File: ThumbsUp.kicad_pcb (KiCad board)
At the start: 2 copper layers, 211.3 x 232.1 mm, 56 parts, among them J1 52559-1233, J1L1 PJ-3200B, J1R1 PJ-3200B, J2 52559-1233, U1 ProMicro

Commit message: v12: Branch: Made the thumb keys reversible - split their hinges, so they could be flipped over.
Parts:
- added H26: MountingHole_Pad, MountingHole:MountingHole_3.5mm_Pad, F.Cu at (55.8, 123.8)
- added H28: MountingHole_Pad, MountingHole:MountingHole_3.5mm_Pad, F.Cu at (71.2, 123.8)
- added H29: MountingHole_Pad, MountingHole:MountingHole_3.5mm_Pad, F.Cu at (55.7, 253.8)
- added H30: MountingHole_Pad, MountingHole:MountingHole_3.5mm_Pad, F.Cu at (71.2, 253.8)
- added MX1: SwE, footprints:SW_D2FC_OMR, F.Cu at (55.8, 114.6)
- added MX2: SwU, footprints:SW_D2FC_OMR, F.Cu at (71.3, 114.6)
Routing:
- net GND-P: track 44.5 -> 0.00 mm, vias 2 -> 0
- net (no net): track 0.00 -> 44.5 mm, vias 0 -> 2
- net GND: track 602.3 -> 633.8 mm
- net SwU: track 64.1 -> 86.9 mm
- net SwE: track 61.1 -> 80.2 mm
- net GNDA: track 222.5 -> 217.5 mm
- removed copper zone on B.Cu, net GND-P
- removed copper zone on F.Cu, net GND-P
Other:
- board size 211.3 x 232.1 mm -> 211.3 x 242.6 mm
- board text added: "u/ak66666 ThumbsUp! v.12 rev.6 July 2026"
- board text removed: "u/ak66666 ThumbsUp! v.12 rev.5 June 2026"

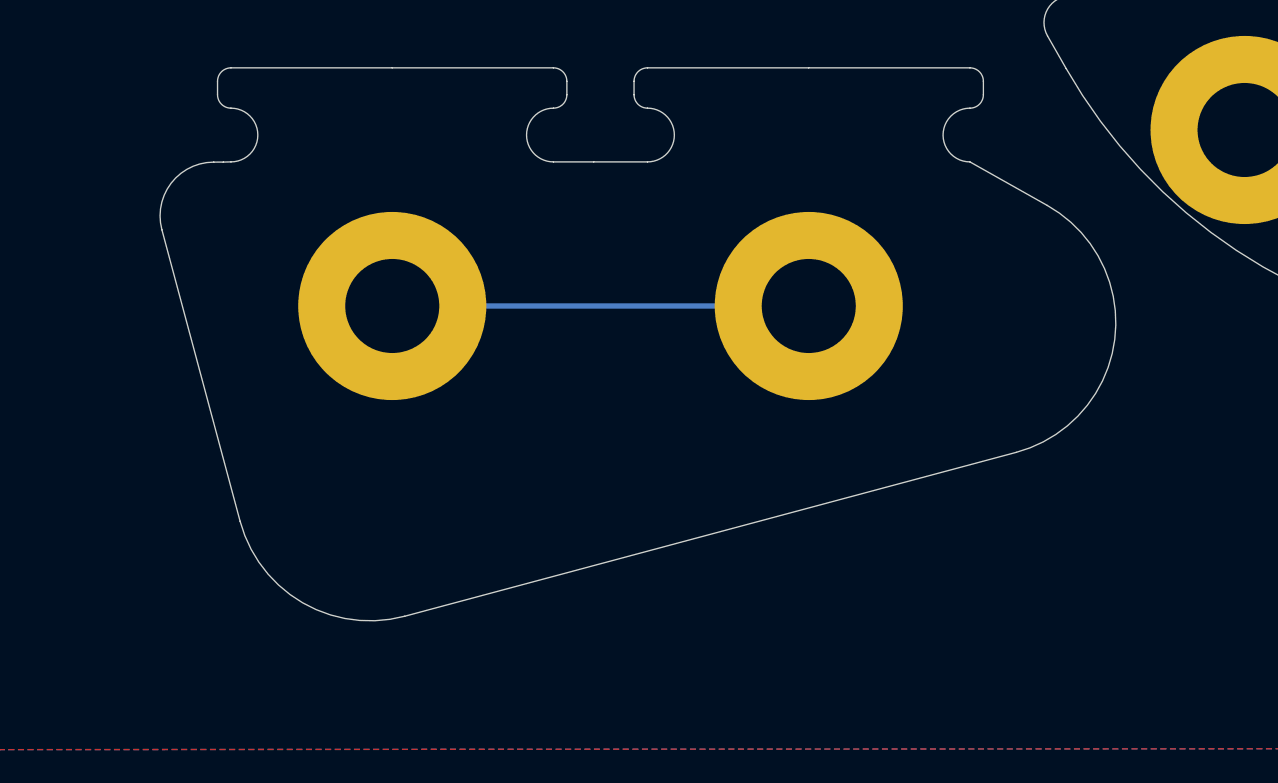
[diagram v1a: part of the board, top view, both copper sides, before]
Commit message: v12: Branch: Made the thumb key hinges replaceable - one board instead of two.
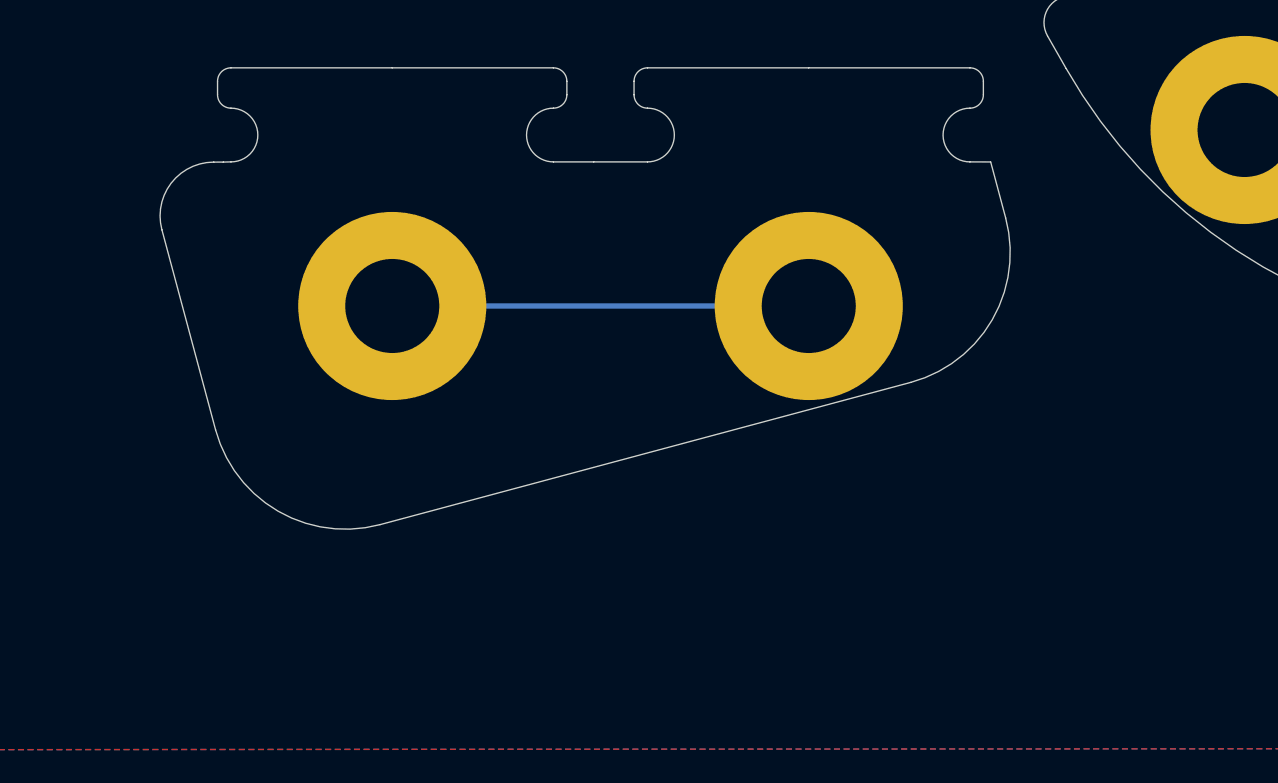
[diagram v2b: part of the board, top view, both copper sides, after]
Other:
- board size 211.3 x 242.6 mm -> 211.3 x 239.2 mm
- board text added: "THIS PCB IS NOT NEEDED, USE THE ONE BELOW FOR THE REVERSED THUMB KEYS"
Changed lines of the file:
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@@
 			)
 			(layer "F.CrtYd")
-			(net 118891357)
 		)
 		(fp_line
@@
 			)
 			(layer "F.CrtYd")
-			(net 118891357)
 		)
 		(fp_line
@@
 			)
 			(layer "F.CrtYd")
-			(net 118891357)
 		)
 		(fp_line
@@
 			)
 			(layer "F.CrtYd")
-			(net 118891357)
 		)
 		(fp_line
@@
 			)
 			(layer "F.Fab")
-			(net 118891357)
 		)
 		(fp_line
@@
 			)
 			(layer "F.Fab")
-			(net 118891357)
 		)
 		(fp_line
@@
 			)
 			(layer "F.Fab")
-			(net 118891357)
 		)
 		(fp_line
@@
 			)
 			(layer "F.Fab")
-			(net 118891357)
 		)
 		(fp_line
@@
 			)
 			(layer "F.Fab")
-			(net 118891357)
 		)
 		(fp_line
@@
 			)
 			(layer "F.Fab")
-			(net 118891357)
 		)
 		(fp_line
@@
 			)
 			(layer "F.Fab")
-			(net 118891357)
 		)
 		(fp_line
@@
 			)
 			(layer "F.Fab")
-			(net 118891357)
 		)
 		(fp_poly
@@
 			(fill yes)
 			(layer "F.Fab")
-			(net 118891357)
 		)
 		(fp_text user "*"
@@
 			)
 			(layer "F.CrtYd")
-			(net 118891357)
 		)
 		(fp_line
@@
 			)
 			(layer "F.CrtYd")
-			(net 118891357)
 		)
 		(fp_line
@@
 			)
 			(layer "F.CrtYd")
-			(net 118891357)
 		)
 		(fp_line
@@
 			)
 			(layer "F.CrtYd")
-			(net 118891357)
 		)
 		(fp_line
@@
 			)
 			(layer "F.Fab")
-			(net 118891357)
 		)
 		(fp_line
@@
 			)
 			(layer "F.Fab")
-			(net 118891357)
 		)
 		(fp_line
@@
 			)
 			(layer "F.Fab")
-			(net 118891357)
 		)
 		(fp_line
@@
 			)
 			(layer "F.Fab")
-			(net 118891357)
 		)
 		(fp_line
@@
 			)
 			(layer "F.Fab")
-			(net 118891357)
 		)
 		(fp_line
@@
 			)
 			(layer "F.Fab")
-			(net 118891357)
 		)
 		(fp_line
@@
 			)
 			(layer "F.Fab")
-			(net 118891357)
 		)
 		(fp_line
@@
 			)
 			(layer "F.Fab")
-			(net 118891357)
 		)
 		(fp_poly
@@
 			(fill yes)
 			(layer "F.Fab")
-			(net 118891357)
 		)
 		(fp_text user "*"
@@
 			(fill no)
 			(layer "Cmts.User")
-			(net 118891357)
 		)
 		(fp_circle
@@
 			(fill no)
 			(layer "F.CrtYd")
-			(net 118891357)
 		)
 		(fp_text user "${REFERENCE}"
@@
 			(fill no)
 			(layer "Cmts.User")
-			(net 118891357)
 		)
 		(fp_circle
@@
 			(fill no)
 			(layer "F.CrtYd")
-			(net 118891357)
 		)
 		(fp_text user "${REFERENCE}"
@@
 	)
 	(gr_arc
-		(start 80.129555 250.009425)
-		(mid 82.638051 254.992037)
-		(end 78.971608 259.196337)
-		(stroke
-			(width 0.05)
-			(type default)
-		)
-		(layer "Edge.Cuts")
-	)
-	(gr_arc
 		(start 114.968747 236.203553)
 		(mid 114.61518 236.05712)
@@
 	)
 	(gr_line
+		(start 78.02 248.39)
+		(end 78.577267 250.471467)
+		(stroke
+			(width 0.05)
+			(type default)
+		)
+		(layer "Edge.Cuts")
+	)
+	(gr_line
 		(start 120.968747 234.703553)
 		(end 114.968747 234.703553)
@@
 		(layer "Edge.Cuts")
 	)
-	(gr_line
-		(start 77.248 248.38772)
-		(end 80.129555 250.009425)
-		(stroke
-			(width 0.05)
-			(type default)
-		)
-		(layer "Edge.Cuts")
-	)
 	(gr_arc
 		(start 231.3 133.9)
@@
 	)
 	(gr_line
-		(start 50.08804 261.761925)
+		(start 49.173356 258.352387)
 		(end 47.177628 250.913603)
 		(stroke
@@
 	)
 	(gr_line
+		(start 77.248 248.38772)
+		(end 78.02 248.39)
+		(stroke
+			(width 0.05)
+			(type default)
+		)
+		(layer "Edge.Cuts")
+	)
+	(gr_line
 		(start 87.468747 238.703553)
 		(end 81.468747 238.703553)
@@
 		(layer "Edge.Cuts")
 	)
-	(gr_arc
-		(start 56.211595 265.295958)
-		(mid 52.418028 264.796943)
-		(end 50.088041 261.761925)
-		(stroke
-			(width 0.05)
-			(type default)
-		)
-		(layer "Edge.Cuts")
-	)
 	(gr_line
 		(start 218.8 91.4)
@@
 	)
 	(gr_arc
+		(start 55.296949 261.886326)
+		(mid 51.503383 261.387363)
+		(end 49.173356 258.352387)
+		(stroke
+			(width 0.05)
+			(type default)
+		)
+		(layer "Edge.Cuts")
+	)
+	(gr_arc
 		(start 160.468747 242.703553)
 		(mid 160.822287 242.850013)
@@
 	)
 	(gr_arc
+		(start 78.577267 250.471467)
+		(mid 78.077353 254.264864)
+		(end 75.041832 256.594096)
+		(stroke
+			(width 0.05)
+			(type default)
+		)
+		(layer "Edge.Cuts")
+	)
+	(gr_arc
 		(start 148.4683 174.5)
 		(mid 149.4683 175.5)
@@
 	)
 	(gr_line
-		(start 78.971608 259.196337)
-		(end 56.211595 265.295957)
+		(start 75.041832 256.594096)
+		(end 55.296949 261.886326)
 		(stroke
 			(width 0.05)
@@
 		)
 	)
+	(gr_text "THIS PCB IS NOT NEEDED,\nUSE THE ONE BELOW \nFOR THE REVERSED THUMB KEYS"
+		(at 19.54 222.66 0)
+		(layer "Edge.Cuts")
+		(effects
+			(font
+				(size 1 1)
+				(thickness 0.15)
+			)
+			(justify left bottom)
+		)
+	)

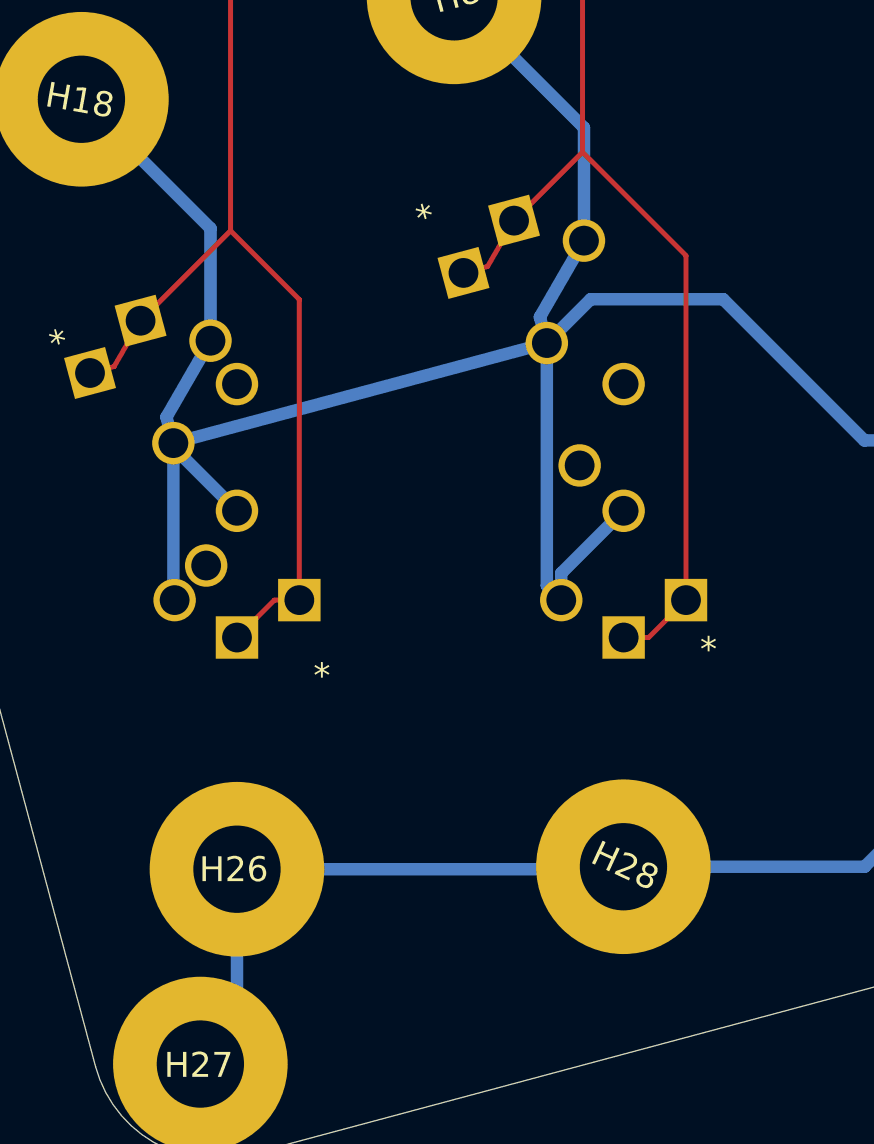
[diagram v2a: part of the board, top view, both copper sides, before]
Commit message: v12: Branch: Shifted the reversed thumb keys 1.5 down to fit the key paddles, there was not enough space.
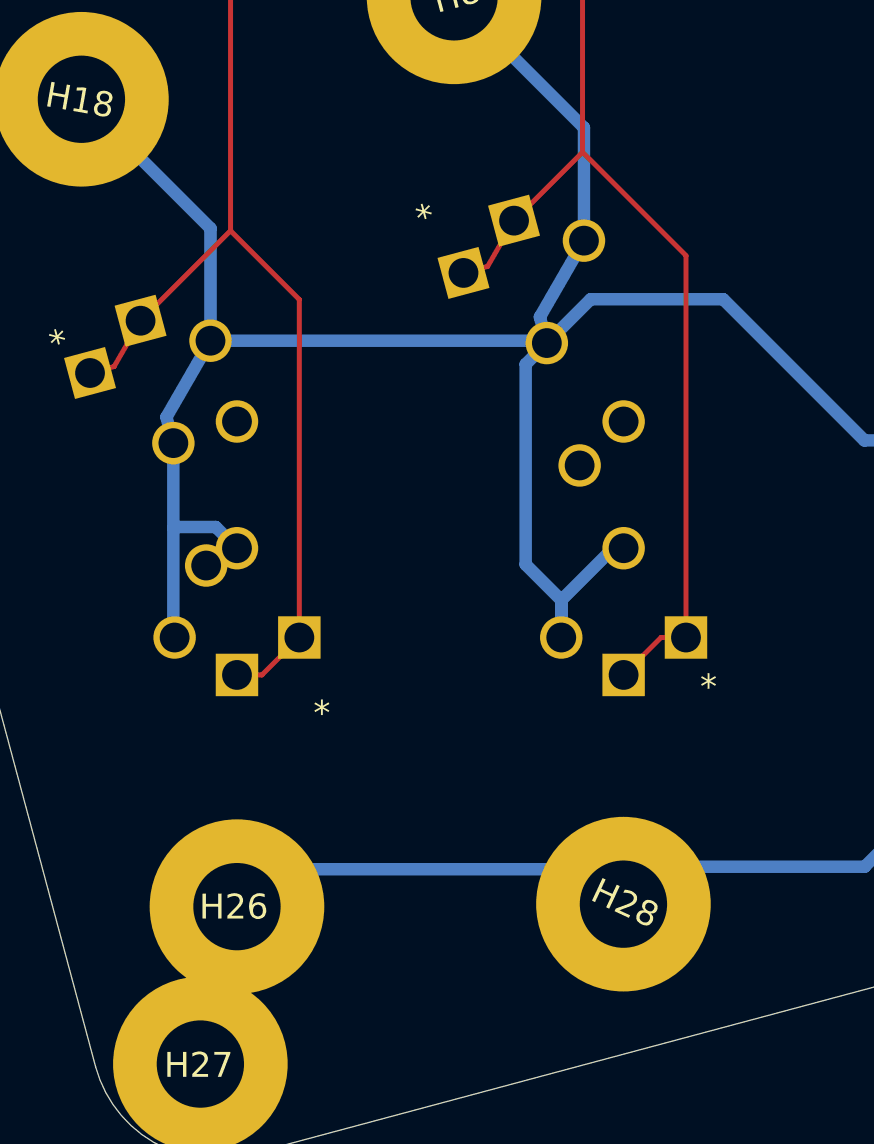
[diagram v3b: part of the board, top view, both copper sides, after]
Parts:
- moved H26 1.50 mm to (55.8, 125.3)
- moved H28 1.50 mm to (71.2, 125.2)
- moved MX1 1.50 mm to (55.8, 116.1)
- moved MX2 1.50 mm to (71.3, 116.1)
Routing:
- net SwE: track 80.2 -> 81.7 mm
- net SwU: track 86.9 -> 88.4 mm
- net GND: track 633.8 -> 634.9 mm

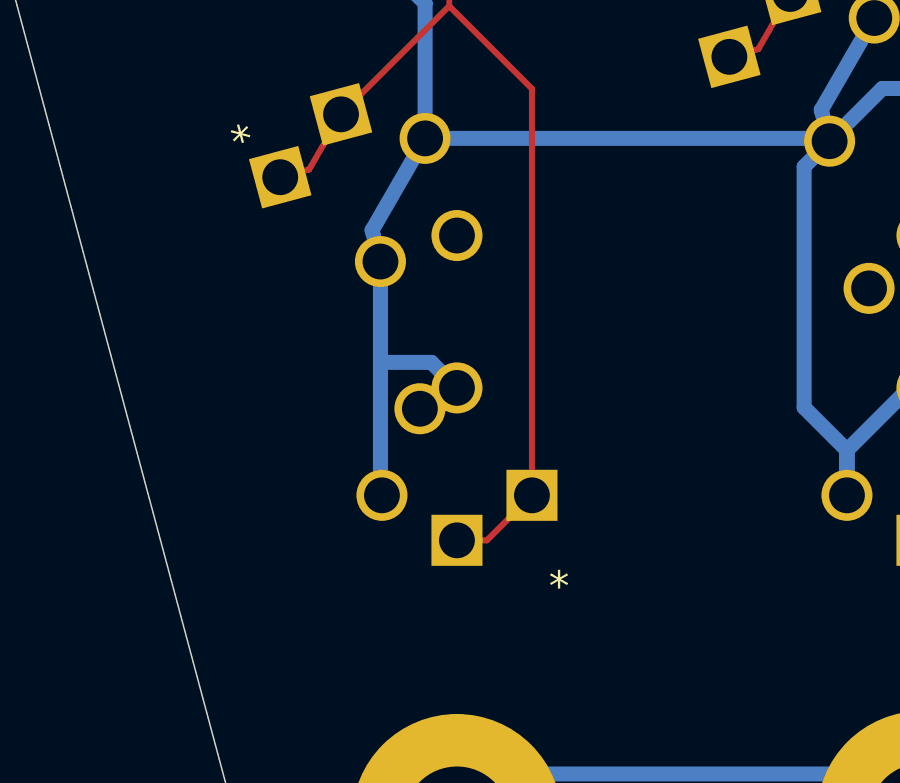
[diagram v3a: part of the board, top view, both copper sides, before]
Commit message: v12: Branch: Moved I-E switch up to avoid overlapping of pin 3 (NC) and pin 2 (NO), which would keep that button always pressed.
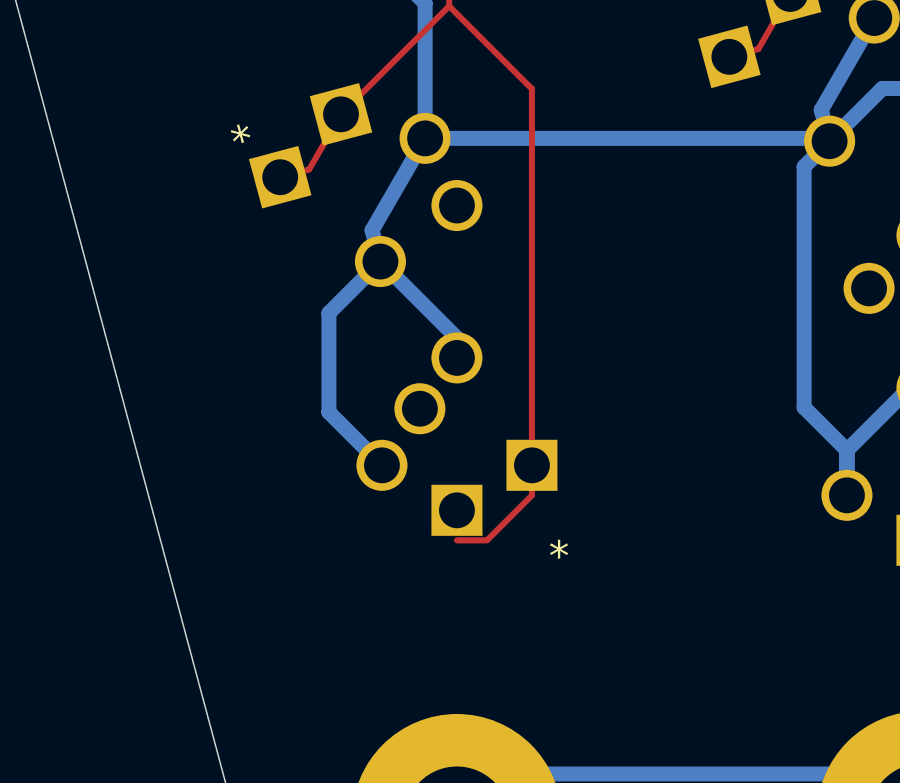
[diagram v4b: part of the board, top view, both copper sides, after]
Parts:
- moved MX1 1.00 mm to (55.8, 115.1)
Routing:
- net GND: track 634.9 -> 636.6 mm
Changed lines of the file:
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@@
 	(footprint "footprints:SW_D2FC_OMR"
 		(layer "F.Cu")
-		(at 55.75721 116.061002 180)
+		(at 55.75721 115.061002 180)
 		(tags "D2FC-7 ")
 		(property "Reference" "MX1"
@@
 	)
 	(segment
+		(start 51.49 111.793792)
+		(end 51.49 108.485366)
+		(width 0.5)
+		(layer "B.Cu")
+		(net 2)
+	)
+	(segment
 		(start 85 114.7317)
 		(end 87.4683 117.2)
@@
 	)
 	(segment
-		(start 53.247328 110.130102)
-		(end 53.20743 110.17)
+		(start 51.49 108.485366)
+		(end 53.20743 106.767936)
 		(width 0.5)
 		(layer "B.Cu")
@@
 	)
 	(segment
-		(start 54.90631 110.130102)
-		(end 53.247328 110.130102)
-		(width 0.5)
-		(layer "B.Cu")
-		(net 2)
-	)
-	(segment
 		(start 87.5 103)
 		(end 87.5 103.08)
@@
 	)
 	(segment
+		(start 55.75721 109.317716)
+		(end 53.20743 106.767936)
+		(width 0.5)
+		(layer "B.Cu")
+		(net 2)
+	)
+	(segment
 		(start 128.16 102.08)
 		(end 134 102.08)
@@
 	)
 	(segment
+		(start 53.25721 113.561002)
+		(end 51.49 111.793792)
+		(width 0.5)
+		(layer "B.Cu")
+		(net 2)
+	)
+	(segment
 		(start 121 99.08)
 		(end 125.16 99.08)
@@
 	)
 	(segment
-		(start 53.20743 106.767936)
-		(end 53.20743 110.17)
-		(width 0.5)
-		(layer "B.Cu")
-		(net 2)
-	)
-	(segment
 		(start 105.5 37)
 		(end 105.5 28.9817)
@@
 	)
 	(segment
-		(start 55.75721 110.981002)
-		(end 54.90631 110.130102)
-		(width 0.5)
-		(layer "B.Cu")
-		(net 2)
-	)
-	(segment
 		(start 55.75721 123.849999)
 		(end 71.150001 123.849999)
@@
 	)
 	(segment
-		(start 53.20743 114.511222)
-		(end 53.25721 114.561002)
-		(width 0.5)
-		(layer "B.Cu")
-		(net 2)
-	)
-	(segment
 		(start 134 102.08)
 		(end 139 107.08)
@@
 	)
 	(segment
+		(start 55.75721 109.981002)
+		(end 55.75721 109.317716)
+		(width 0.5)
+		(layer "B.Cu")
+		(net 2)
+	)
+	(segment
 		(start 67.33 111.63379)
 		(end 68.757212 113.061002)
@@
 		(width 0.5)
 		(layer "B.Cu")
-		(net 2)
-	)
-	(segment
-		(start 53.20743 110.17)
-		(end 53.20743 114.511222)
-		(width 0.5)
-		(layer "B.Cu")
